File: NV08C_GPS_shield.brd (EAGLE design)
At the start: 100 x 80 mm, 43 parts, among them IC1 74LVC1T45SOT23-HAND, IC2 74LVC1T45SOT23-HAND, IC3 74LVC1T45SOT23-HAND, IC4 74LVC1T45SOT23-HAND, IC5 74LVC1T45SOT23-HAND, IC6 74LVC1T45SOT23-HAND, IC7 MCP1702-3.3, X1 CONN-SMATHD-SMD-EDGE

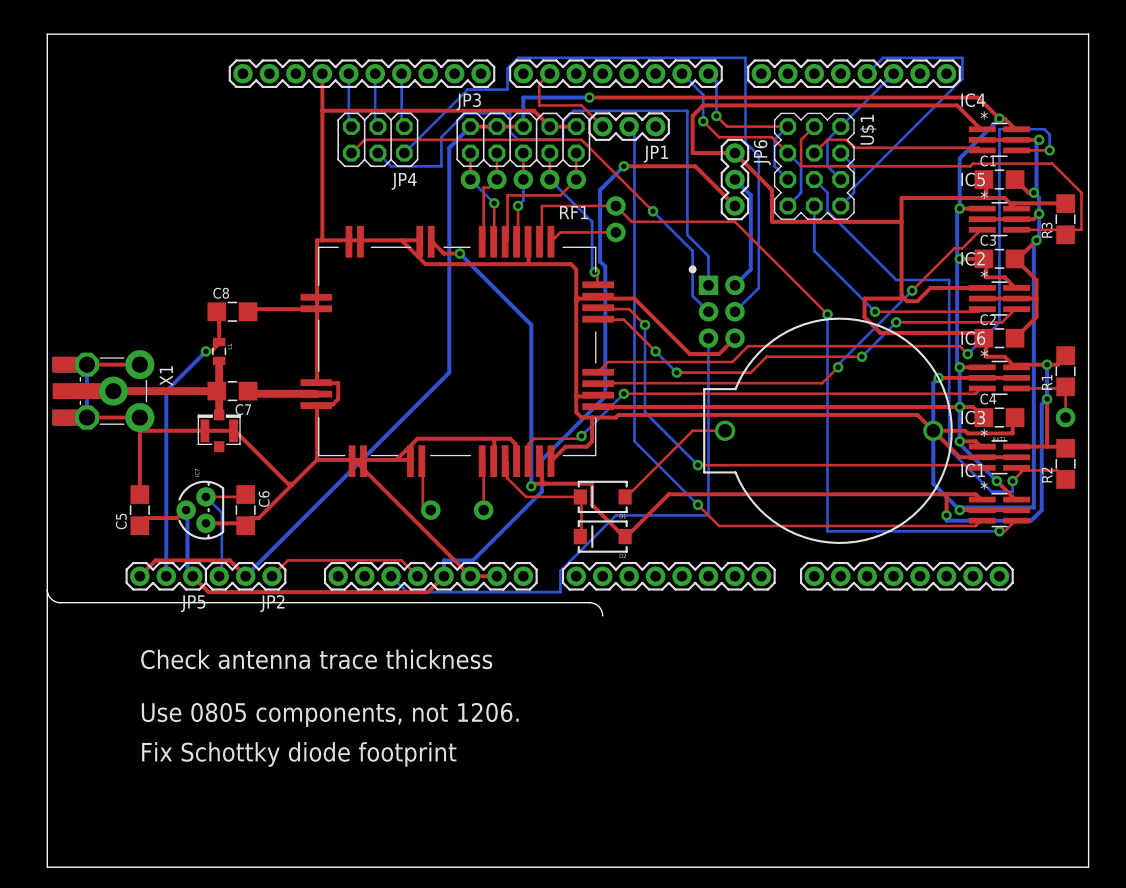
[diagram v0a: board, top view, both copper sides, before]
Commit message: Changed BAS32L to BAV70.
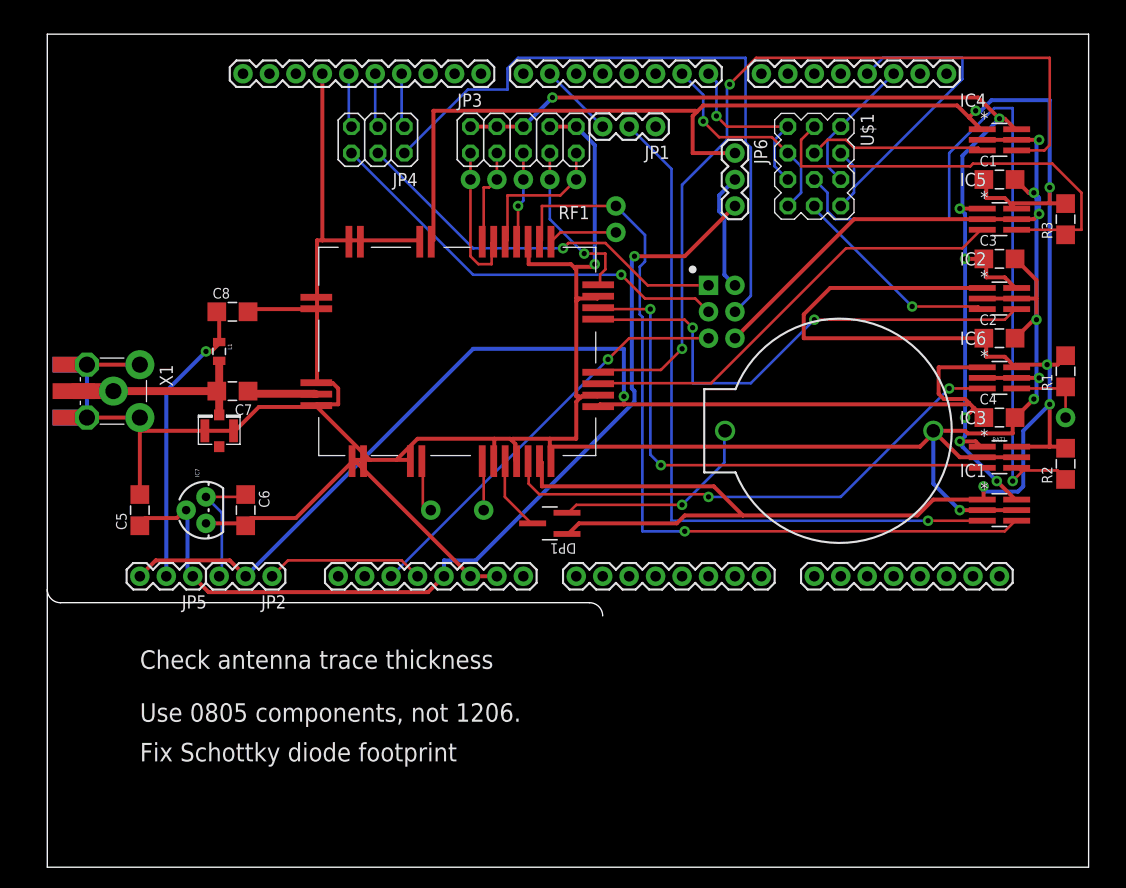
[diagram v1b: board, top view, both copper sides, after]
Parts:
- removed D1, D2: DIODE-SCHOTTKY_, SteveMarple:SMA-DIODE
- added DP1: BAV70, SteveMarple:SOT23-3-HAND
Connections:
- net IOREF: now also DP1.1; no longer D2.A
- net VBAT: now also DP1.3; no longer D1.C, D2.C
- net VBATT: now also DP1.2; no longer D1.A
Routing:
- net IOREF: track 237.7 -> 261.7 mm
- net N$12: track 50.4 -> 73.0 mm
- net GND: track 401.2 -> 381.8 mm, vias 6 -> 8
- net MISO: track 55.9 -> 37.4 mm, vias 0 -> 1
- net N$2: track 52.4 -> 39.9 mm, vias 0 -> 1
- net GPS_TX2: track 69.4 -> 79.8 mm
- net +5V: track 98.1 -> 89.2 mm
- net VBATT: track 12.2 -> 20.2 mm, vias 0 -> 1
- net VBAT: track 13.6 -> 7.16 mm
- net +3V3: track 212.8 -> 218.9 mm
- net GPIO3: track 9.47 -> 14.5 mm, vias 1 -> 0
- net GPIO1: track 74.7 -> 79.8 mm, vias 2 -> 1
- net GPS_TX1: track 44.8 -> 48.8 mm, vias 4 -> 2
- net SCK: track 44.2 -> 40.6 mm
- net GPS_RX1: track 48.2 -> 51.4 mm
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
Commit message: Switching to 0805 packages for some parts.
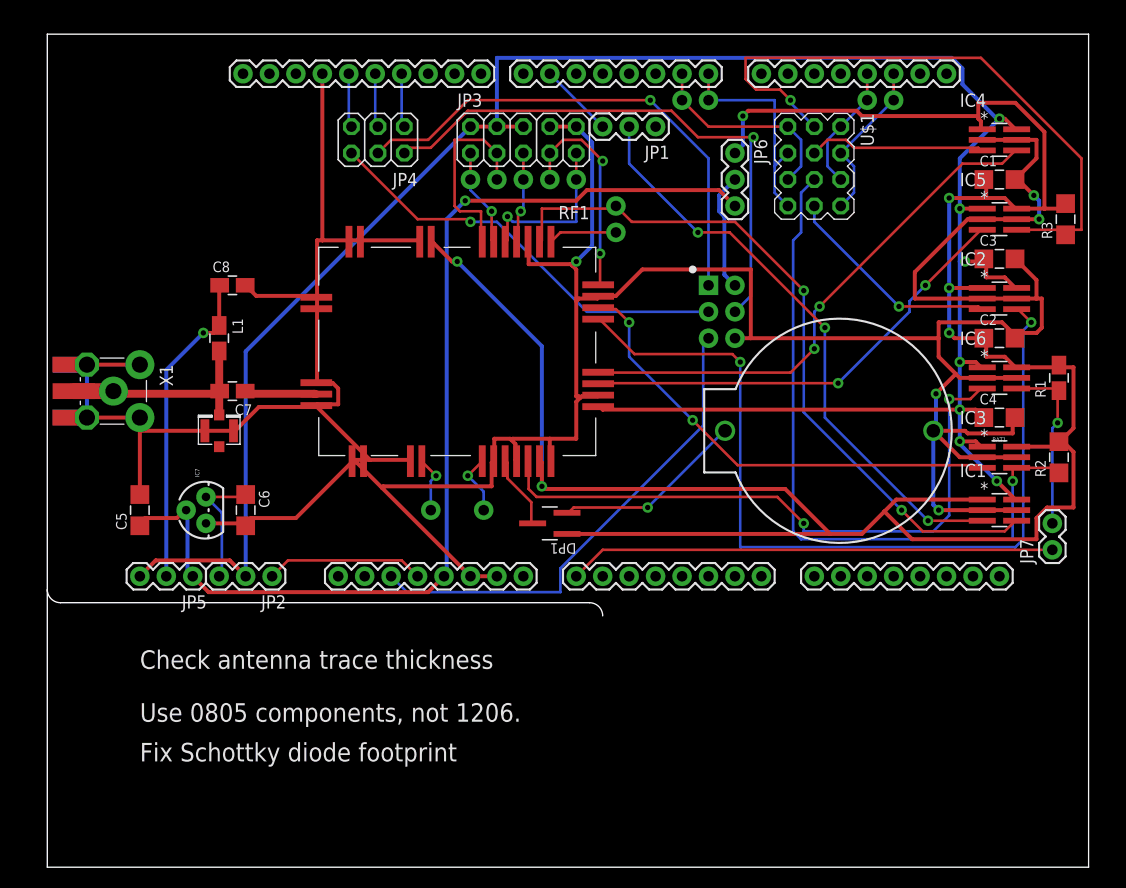
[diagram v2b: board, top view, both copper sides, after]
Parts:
- removed U$2: PAD, SteveMarple:PAD
- added JP7: (no value), SparkFun:1X02
- added U$14, U$15, U$16, U$17: PAD, SteveMarple:PAD
- C7, C8, R1: device SteveMarple:1206-HAND -> SteveMarple:0805-HAND
- L1: device SteveMarple:0805 -> SteveMarple:0805-HAND
- moved C8 2.54 mm to (17.8, 55.9)
- moved L1 1.27 mm to (16.5, 50.8)
- moved R1 0.90 mm to (97.2, 47.0)
- moved R2 0.90 mm to (97.2, 39.4)
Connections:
- new net A0: JP7.1, U$11.A0
- net N$8: now also JP7.2; no longer U$2.1
- net RX0: now also U$1.10, U$1.12, U$14.1; no longer U$1.11, U$1.9
- net RX1: now also U$1.2, U$1.4, U$16.1; no longer U$1.1, U$1.3
- net TX0: now also U$1.11, U$1.9, U$15.1; no longer U$1.10, U$1.12
- net TX1: now also U$1.1, U$1.3, U$17.1; no longer U$1.2, U$1.4
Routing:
- net A0: track 0.00 -> 46.8 mm
- net GPS_TX1: track 48.8 -> 83.7 mm
- net IOREF: track 261.7 -> 231.9 mm, vias 5 -> 6
- net GPS_TX2: track 79.8 -> 51.1 mm
- net TX1: track 32.7 -> 12.3 mm
- net N$6: track 43.4 -> 61.1 mm, vias 0 -> 1
- net PPS: track 69.4 -> 56.7 mm, vias 1 -> 3
- net +5V: track 89.2 -> 101.1 mm
- net MISO: track 37.4 -> 48.4 mm
- net GPIO1: track 79.8 -> 69.4 mm, vias 1 -> 2
- net !GPS_RESET: track 50.6 -> 60.6 mm
- net GPIO4: track 9.40 -> 19.2 mm
- net N$8: track 7.65 -> 17.2 mm, vias 0 -> 1
- net MOSI: track 63.0 -> 53.8 mm, vias 0 -> 1
- net N$2: track 39.9 -> 47.2 mm, vias 1 -> 0
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
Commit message: Layout changes and some missing pin connections made.
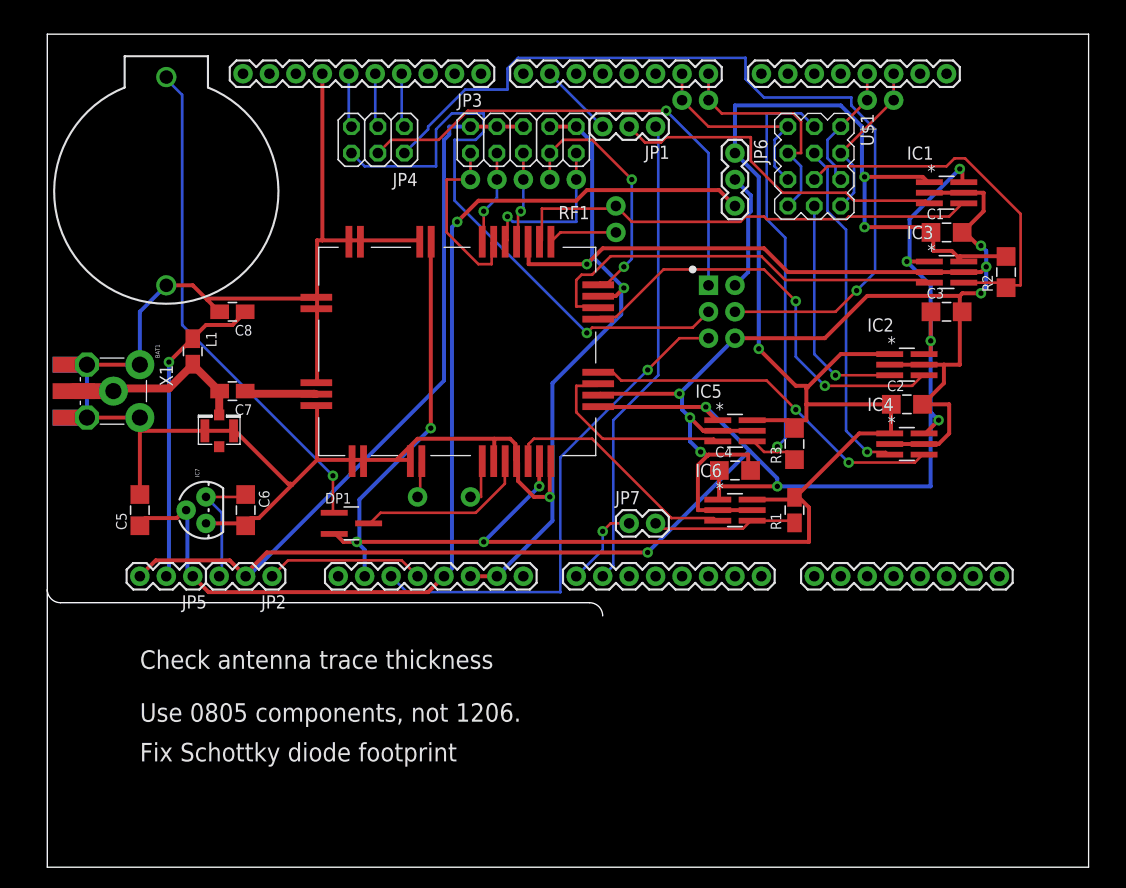
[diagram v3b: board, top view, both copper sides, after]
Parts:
- moved BAT1 75.0 mm to (11.4, 55.9), turned to 90 degrees
- moved JP7 40.7 mm to (55.9, 33.0), turned to 0 degrees
- moved R3 33.8 mm to (71.8, 40.6)
- moved IC5 32.5 mm to (66.0, 41.9)
- moved IC1 30.9 mm to (86.4, 64.8)
- moved IC4 30.5 mm to (82.5, 40.6)
- moved R1 28.4 mm to (71.8, 34.3)
- moved IC6 28.4 mm to (66.0, 34.3)
- moved C4 25.9 mm to (66.0, 38.1)
- moved DP1 19.0 mm to (29.2, 33.0), turned to 0 degrees
- moved IC3 18.5 mm to (86.4, 57.1)
- moved R2 18.5 mm to (92.1, 57.1)
- moved IC2 10.9 mm to (82.5, 48.3)
- moved C2 10.9 mm to (82.5, 44.5)
- moved C1 7.18 mm to (86.4, 61.0)
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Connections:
- removed net N$11: JP1.1
- new net A1: JP1.1, U$11.A1
- net IOREF: now also DP1.2, U$11.IOREF; no longer DP1.1
- net VBATT: now also DP1.1; no longer DP1.2
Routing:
- net A1: track 0.00 -> 45.5 mm
- net GPS_TX1: track 83.7 -> 41.5 mm
- net A0: track 46.8 -> 8.23 mm, vias 0 -> 1
- net !GPS_RESET: track 60.6 -> 23.3 mm, vias 2 -> 0
- net N$12: track 67.6 -> 35.6 mm, vias 1 -> 0
- net VBATT: track 18.4 -> 48.6 mm
- net MOSI: track 53.8 -> 83.6 mm
- net GPS_RX2: track 43.6 -> 19.5 mm, vias 2 -> 0
- net GPIO1: track 69.4 -> 45.7 mm, vias 2 -> 0
- net PPS: track 56.7 -> 33.6 mm, vias 3 -> 0
- net SCK: track 40.6 -> 58.6 mm
- net N$6: track 61.1 -> 43.5 mm
- net N$13: track 17.1 -> 33.1 mm, vias 0 -> 1
- net GPS_TX2: track 51.1 -> 35.2 mm
- net GND: track 376.0 -> 388.5 mm, vias 5 -> 9
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
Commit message: Adding protection resistors in GPS TX lines.
Enables the same UART to be used to access the bootloader during the boot
sequence without damaging the level shifters or external FTDI device.
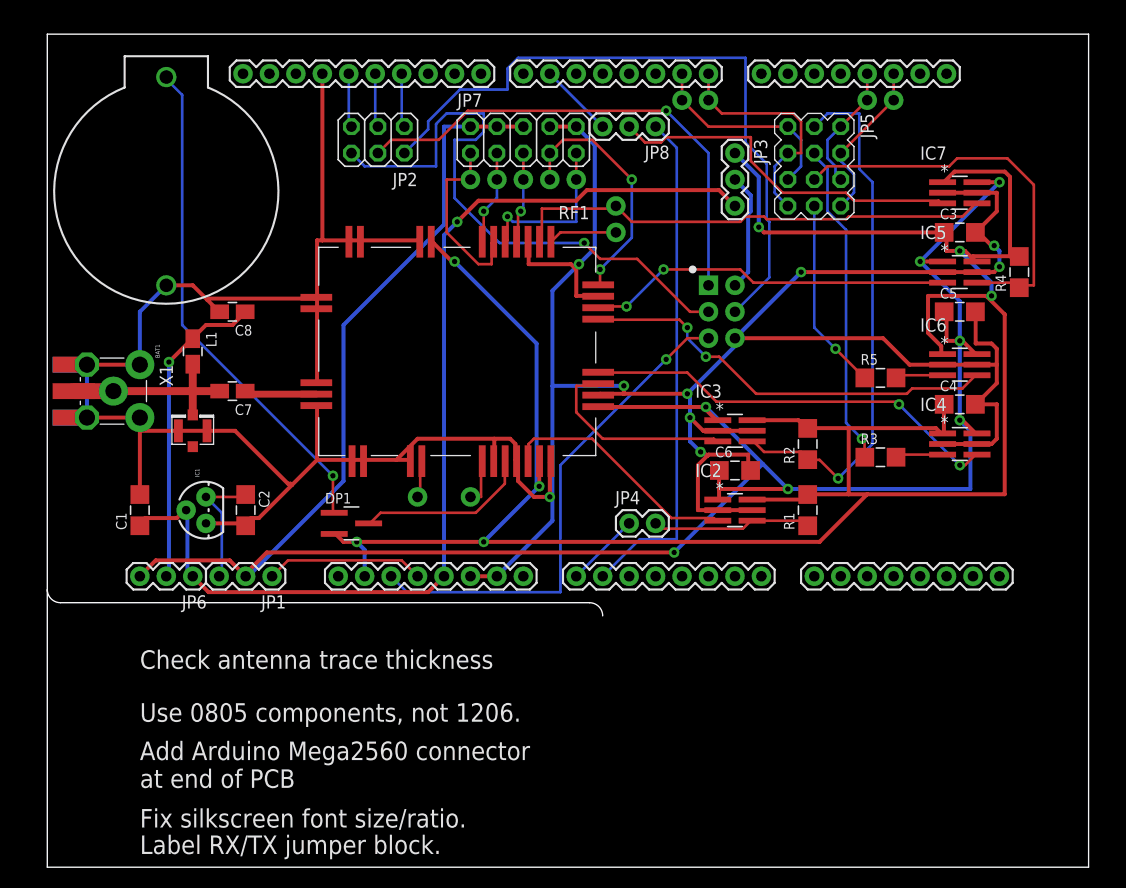
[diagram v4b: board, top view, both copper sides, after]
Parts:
- removed U$16, U$17: PAD, SteveMarple:PAD
- added JP8: (no value), SparkFun:1X03
- added R4: 100k, SteveMarple:1206-HAND
- added R5: 10k, SteveMarple:1206-HAND
- added U$2: PAD, SteveMarple:PAD
- C1, C2: value 100n -> 1u
- C5, C6: value 1u -> 100n
- IC1: value 74LVC1T45SOT23-HAND -> MCP1702-3.3; device SteveMarple:SOT23-6-HAND -> SteveMarple:TO-92
- IC7: value MCP1702-3.3 -> 74LVC1T45SOT23-HAND; device SteveMarple:TO-92 -> SteveMarple:SOT23-6-HAND
- JP1: value (none) -> 3V3 SRC
- JP2: value 3V3 SRC -> ALT ISP; device SparkFun:1X03 -> pinhead:2X03
- JP3: value (none) -> ISP VCC; device pinhead:2X05 -> SparkFun:1X03
- JP4: value ALT ISP -> (none); device pinhead:2X03 -> SparkFun:1X02
- JP5: value V ANT -> PIN_3X4; device SparkFun:1X03 -> pinhead_3row:PIN_3X4
- JP6: value ISP VCC -> V ANT
- JP7: device SparkFun:1X02 -> pinhead:2X05
- R1: device SteveMarple:0805-HAND -> SteveMarple:1206-HAND
- R3: value 100k -> 10k
- U$1: value PIN_3X4 -> PAD; device pinhead_3row:PIN_3X4 -> SteveMarple:PAD
- U$10: value PAD -> ?
- U$11: value CALUNIUM-SHIELD-V3V3-NO-HOLES-NO-TEXT -> PAD; device SteveMarple:CALUNIUM-SHIELD-NO-OUTLINE-NO-HOLES-NO-TEXT-V3 -> SteveMarple:PAD
- U$13: value U.FL -> PAD; device SparkFun:U.FL -> SteveMarple:PAD
- U$5: value PAD -> CALUNIUM-SHIELD-V3V3-NO-HOLES-NO-TEXT; device SteveMarple:PAD -> SteveMarple:CALUNIUM-SHIELD-NO-OUTLINE-NO-HOLES-NO-TEXT-V3
- U$7: value PAD -> U.FL; device SteveMarple:PAD -> SparkFun:U.FL
- U$8: value ? -> PAD
- moved C1 81.9 mm to (8.89, 34.3), turned to 90 degrees
- moved C5 81.0 mm to (87.6, 53.3), turned to 0 degrees
- moved IC7 78.5 mm to (87.6, 64.8), turned to 0 degrees
- moved JP5 77.5 mm to (77.5, 72.4), turned to 270 degrees
- moved IC1 77.4 mm to (15.2, 34.3), turned to 90 degrees
- moved JP6 66.1 mm to (14.0, 27.9), turned to 180 degrees
- moved C2 64.3 mm to (19.1, 34.3), turned to 270 degrees
- moved JP1 56.8 mm to (21.6, 27.9)
- moved C6 47.1 mm to (66.0, 38.1), turned to 0 degrees
- moved JP4 44.0 mm to (55.9, 33.0), turned to 0 degrees
- moved JP2 43.1 mm to (31.8, 69.8)
- moved JP7 38.2 mm to (45.7, 69.8)
- moved U$13 37.9 mm to (45.7, 66.0), turned to 270 degrees
- moved U$7 36.0 mm to (14.0, 41.9), turned to 90 degrees
- moved U$10 31.8 mm to (54.6, 61.0)
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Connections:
- new net N$3: IC4.3, R3.2
- new net N$5: IC6.3, R5.2
- net !GPS_RESET: now also IC2.3; no longer IC6.3
- net +3V3: now also C5.1, C6.1, IC2.1, IC6.6, IC7.6, JP1.2, JP6.3, JP7.2, JP7.4, JP7.6; no longer C3.1, C4.1, IC1.6, IC2.6, IC6.1, JP2.2, JP3.2, JP3.4, JP3.6, JP5.3
- net +5V: now also C1.1, IC1.2, JP3.3, JP6.1, U$5.5V; no longer C5.1, IC7.2, JP5.1, JP6.3, U$11.5V
- net 11: now also JP2.1, U$5.11@0; no longer JP4.1, U$11.11@0
- net 12: now also JP2.3, U$5.12@0; no longer JP4.3, U$11.12@0
- net 13: now also JP2.5, U$5.13@0; no longer JP4.5, U$11.13@0
- net 3V3_SHIELD: now also JP1.1, U$5.3.3V; no longer JP2.1, U$11.3.3V
- net 6: now also JP8.3, U$5.6; no longer JP1.3, U$11.6
- net A0: now also JP4.1, U$5.A0; no longer JP7.1, U$11.A0
- net A1: now also JP8.1, U$5.A1; no longer JP1.1, U$11.A1
- net GND: now also IC1.1, IC7.2, IC7.5, JP7.10, JP7.8, U$5.GND@0, U$5.GND@1, U$5.GND@2, U$5.GND@3, U$7.P$1, U$7.P$2; no longer IC1.2, IC1.5, IC7.1, JP3.10, JP3.8, U$11.GND@0, U$11.GND@1, U$11.GND@2, U$11.GND@3, U$13.P$1, U$13.P$2
- net GPIO0: now also U$8.1; no longer U$10.1
- net GPIO1: now also IC7.4; no longer IC1.4
- net GPIO2: now also U$10.1; no longer U$8.1
- net GPIO3: now also JP7.1, U$11.1; no longer JP3.1, U$7.1
- net GPIO4: now also JP7.3, U$12.1; no longer JP3.3, U$6.1
- net GPIO5: now also JP7.5, U$13.1; no longer JP3.5, U$5.1
- net GPIO6: now also JP7.7, U$14.1; no longer JP3.7, U$4.1
- net GPIO7: now also JP7.9, U$15.1; no longer JP3.9, U$3.1
- net GPS_RX1: now also IC5.3; no longer IC3.3
- net GPS_RX2: now also IC3.3; no longer IC5.3
- net GPS_TX1: now also IC6.4; no longer IC2.4
- net IOREF: now also C3.1, C4.1, IC2.6, IC6.1, IC7.1, JP3.1, R4.2, U$5.IOREF; no longer C1.1, C2.1, IC1.1, IC2.1, IC6.6, JP6.1, R3.2, U$11.IOREF
- net ISP_VCC: now also JP3.2, U$5.ISP_VCC; no longer JP6.2, U$11.ISP_VCC
- net MISO: now also JP2.4, U$5.ISP_MISO; no longer JP4.4, U$11.ISP_MISO
- net MOSI: now also JP2.2, U$5.ISP_MOSI; no longer JP4.2, U$11.ISP_MOSI
- net N$1: now also C2.1, IC1.3, JP1.3; no longer C6.1, IC7.3, JP2.3
- net N$12: now also IC5.4, JP5.7, R4.1; no longer IC3.4, R2.1, U$1.7
- net N$13: now also JP5.6, R3.1; no longer IC4.3, U$1.6
- net N$15: now also JP5.8, R5.1; no longer IC2.3, U$1.8
- net N$2: now also U$5.!ISP_RESET, U$5.!RESET@0; no longer U$11.!ISP_RESET, U$11.!RESET@0
- net N$20: now also U$6.1; no longer U$12.1
- net N$4: now also U$7.P$3; no longer U$13.P$3
- net N$6: now also IC3.4, JP5.5, R2.1; no longer IC5.4, R3.1, U$1.5
- net N$8: now also IC2.4, JP4.2; no longer IC6.4, JP7.2
- net PPS: now also IC7.3, JP8.2; no longer IC1.3, JP1.2
- net RX0: now also JP5.10, JP5.12, U$1.1, U$5.0(RX0); no longer U$1.10, U$1.12, U$11.0(RX0), U$14.1
- net RX1: now also JP5.2, JP5.4, U$3.1, U$5.2@1; no longer U$1.2, U$1.4, U$11.2@1, U$16.1
- net SCK: now also JP2.6, U$5.ISP_SCK; no longer JP4.6, U$11.ISP_SCK
- net TX0: now also JP5.11, JP5.9, U$2.1, U$5.1(TX0); no longer U$1.11, U$1.9, U$11.1(TX0), U$15.1
- net TX1: now also JP5.1, JP5.3, U$4.1, U$5.3@1; no longer U$1.1, U$1.3, U$11.3@1, U$17.1
- net V_ANT: now also JP6.2; no longer JP5.2
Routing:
- net MOSI: track 83.6 -> 64.9 mm, vias 1 -> 0
- net IOREF: track 219.4 -> 237.0 mm
- net GND: track 388.5 -> 373.2 mm
- net +3V3: track 214.6 -> 222.7 mm
- net N$6: track 43.5 -> 51.5 mm
- net GPS_RX1: track 40.6 -> 35.1 mm, vias 0 -> 2
- net GPS_TX2: track 35.2 -> 40.5 mm
- net N$3: track 0.00 -> 4.58 mm
- net N$5: track 0.00 -> 4.58 mm
- net N$15: track 22.3 -> 18.5 mm
- net A1: track 45.5 -> 49.1 mm
- net N$12: track 35.6 -> 38.5 mm
- net N$13: track 33.1 -> 31.4 mm
- net SCK: track 58.6 -> 57.1 mm
- net N$8: track 14.0 -> 15.4 mm
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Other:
- board text added: "Add Arduino Mega2560 connector at end of PCB"
- board text added: "Fix silkscreen font size/ratio."
- board text added: "Label RX/TX jumper block."
- board text removed: "Fix Schottky diode footprint"
